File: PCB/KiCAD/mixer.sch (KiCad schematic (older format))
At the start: 12 parts

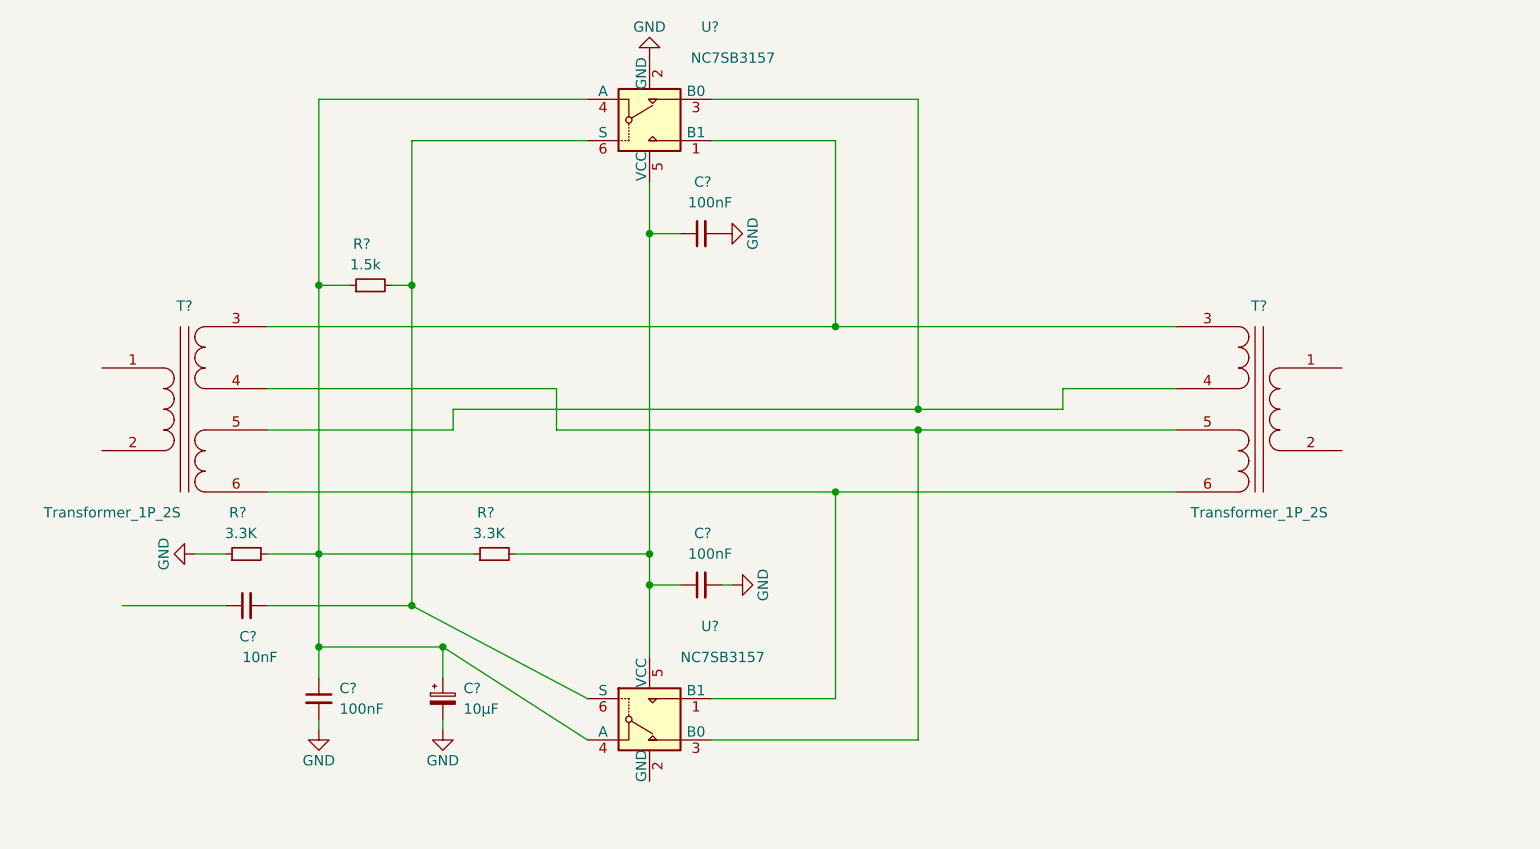
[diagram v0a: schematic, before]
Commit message: mixer schema is done, pcb progress, fix 78l06 issue
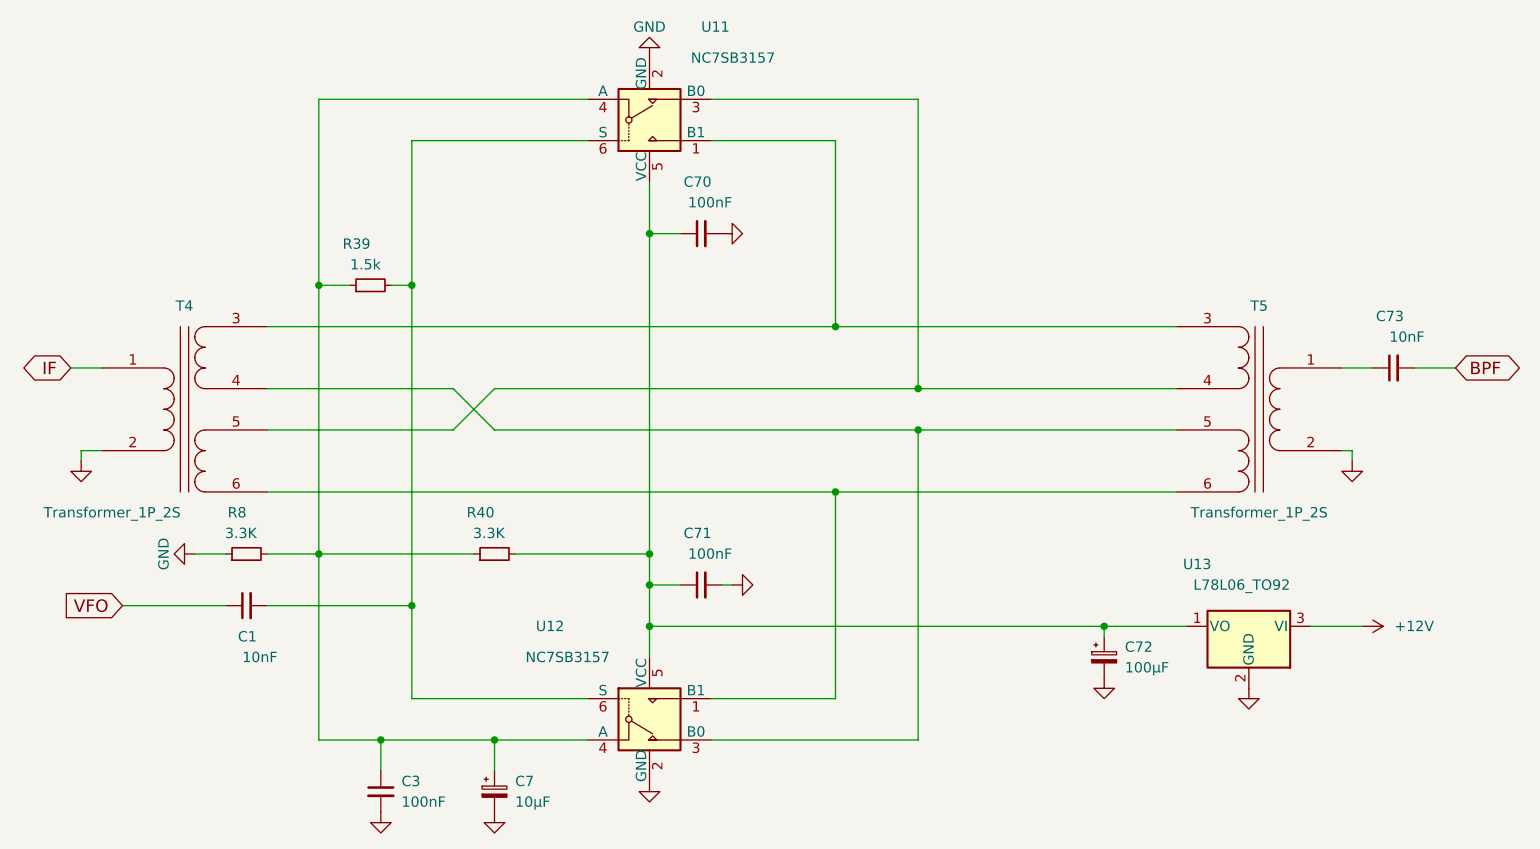
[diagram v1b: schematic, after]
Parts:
- added C72: 100µF, DragonFly:CP_Radial_D6.3mm_P2.50mm, symbol CP_Small
- added C73: 10nF, DragonFly:C_0603_HandSoldering, symbol C_Small
- added U13: L78L06_TO92, DragonFly:TO-92_Molded_Wide_Oval, symbol L78L06_TO92
- C1, C3, C70, C71: renamed from C?; footprint (none) -> DragonFly:C_0603_HandSoldering
- C7: renamed from C?; footprint (none) -> DragonFly:CP_Radial_D4.0mm_P2.00mm
- R39, R40, R8: renamed from R?; footprint (none) -> DragonFly:R_1206_0603
- T4, T5: renamed from T?; footprint (none) -> DragonFly:HF12
- U11, U12: renamed from U?; footprint (none) -> DragonFly:SOT-23-6
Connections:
- net GND: now also T4.2 (AB), T5.2 (AB), U12.2 (GND), C72.2, U13.2 (GND)
- net IF: now reaches T4.1 (AA)
- net at T5.1 (AA): now also C73.1
- net at C70.1, C71.1, R40.2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: now also C72.1, U13.1 (VO)
- net VFO: now reaches C1.1
- new net +12V: U13.3 (VI)
- new net BPF: C73.2
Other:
- moved on the sheet: C3, C7

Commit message: PCB v1.0
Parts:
- C3, C70, C71: footprint DragonFly:C_0603_HandSoldering -> DragonFly:C_1206_0603
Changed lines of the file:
@@
 Connection ~ 4850 3400
 $Comp
-L GND #PWR125
+L GND #PWR128
 U 1 1 612C19B8
 P 2650 3400
-F 0 "#PWR125" H 2650 3150 50  0001 C CNN
+F 0 "#PWR128" H 2650 3150 50  0001 C CNN
 F 1 "GND" H 2650 3250 50  0000 C CNN
 F 2 "" H 2650 3400 50  0001 C CNN
@@
 F 0 "C71" V 5350 3500 50  0000 L CNN
 F 1 "100nF" V 5250 3400 50  0000 L CNN
-F 2 "DragonFly:C_0603_HandSoldering" H 5100 3550 50  0001 C CNN
+F 2 "DragonFly:C_1206_0603" H 5100 3550 50  0001 C CNN
 F 3 "" H 5100 3550 50  0001 C CNN
 	1    5100 3550
@@
 $EndComp
 $Comp
-L GND #PWR131
+L GND #PWR134
 U 1 1 612C2F5C
 P 5250 3550
-F 0 "#PWR131" H 5250 3300 50  0001 C CNN
+F 0 "#PWR134" H 5250 3300 50  0001 C CNN
 F 1 "GND" H 5250 3400 50  0001 C CNN
 F 2 "" H 5250 3550 50  0001 C CNN
@@
 F 0 "C70" V 5350 1800 50  0000 L CNN
 F 1 "100nF" V 5250 1700 50  0000 L CNN
-F 2 "DragonFly:C_0603_HandSoldering" H 5100 1850 50  0001 C CNN
+F 2 "DragonFly:C_1206_0603" H 5100 1850 50  0001 C CNN
 F 3 "" H 5100 1850 50  0001 C CNN
 	1    5100 1850
@@
 	5150 1400 5750 1400
 $Comp
-L GND #PWR130
+L GND #PWR133
 U 1 1 612C37A6
 P 5200 1850
-F 0 "#PWR130" H 5200 1600 50  0001 C CNN
+F 0 "#PWR133" H 5200 1600 50  0001 C CNN
 F 1 "GND" H 5200 1700 50  0001 C CNN
 F 2 "" H 5200 1850 50  0001 C CNN
@@
 	3700 1400 4550 1400
 $Comp
-L GND #PWR128
+L GND #PWR131
 U 1 1 612C38C3
 P 4850 1000
-F 0 "#PWR128" H 4850 750 50  0001 C CNN
+F 0 "#PWR131" H 4850 750 50  0001 C CNN
 F 1 "GND" H 4850 850 50  0000 C CNN
 F 2 "" H 4850 1000 50  0001 C CNN
@@
 	2050 2500 2200 2500
 $Comp
-L GND #PWR124
+L GND #PWR127
 U 1 1 612C7046
 P 2100 2950
-F 0 "#PWR124" H 2100 2700 50  0001 C CNN
+F 0 "#PWR127" H 2100 2700 50  0001 C CNN
 F 1 "GND" H 2100 2800 50  0001 C CNN
 F 2 "" H 2100 2950 50  0001 C CNN
@@
 	2100 2900 2200 2900
 $Comp
-L GND #PWR134
+L GND #PWR137
 U 1 1 612C70EC
 P 8250 2950
-F 0 "#PWR134" H 8250 2700 50  0001 C CNN
+F 0 "#PWR137" H 8250 2700 50  0001 C CNN
 F 1 "GND" H 8250 2800 50  0001 C CNN
 F 2 "" H 8250 2950 50  0001 C CNN
@@
 	8250 2900 8200 2900
 $Comp
-L GND #PWR129
+L GND #PWR132
 U 1 1 612C7167
 P 4850 4500
-F 0 "#PWR129" H 4850 4250 50  0001 C CNN
+F 0 "#PWR132" H 4850 4250 50  0001 C CNN
 F 1 "GND" H 4850 4350 50  0001 C CNN
 F 2 "" H 4850 4500 50  0001 C CNN
@@
 F 0 "C3" H 3650 4600 50  0000 L CNN
 F 1 "100nF" H 3650 4500 50  0000 L CNN
-F 2 "DragonFly:C_0603_HandSoldering" H 3550 4550 50  0001 C CNN
+F 2 "DragonFly:C_1206_0603" H 3550 4550 50  0001 C CNN
 F 3 "" H 3550 4550 50  0001 C CNN
 	1    3550 4550
@@
 Connection ~ 3550 4300
 $Comp
-L GND #PWR127
+L GND #PWR130
 U 1 1 612C7874
 P 4100 4650
-F 0 "#PWR127" H 4100 4400 50  0001 C CNN
+F 0 "#PWR130" H 4100 4400 50  0001 C CNN
 F 1 "GND" H 4100 4500 50  0001 C CNN
 F 2 "" H 4100 4650 50  0001 C CNN
@@
 $EndComp
 $Comp
-L GND #PWR126
+L GND #PWR129
 U 1 1 612C78A6
 P 3550 4650
-F 0 "#PWR126" H 3550 4400 50  0001 C CNN
+F 0 "#PWR129" H 3550 4400 50  0001 C CNN
 F 1 "GND" H 3550 4500 50  0001 C CNN
 F 2 "" H 3550 4650 50  0001 C CNN
@@
 Connection ~ 4850 3750
 $Comp
-L GND #PWR133
+L GND #PWR136
 U 1 1 612C940C
 P 7750 4050
-F 0 "#PWR133" H 7750 3800 50  0001 C CNN
+F 0 "#PWR136" H 7750 3800 50  0001 C CNN
 F 1 "GND" H 7750 3900 50  0001 C CNN
 F 2 "" H 7750 4050 50  0001 C CNN
@@
 $EndComp
 $Comp
-L GND #PWR132
+L GND #PWR135
 U 1 1 612C9675
 P 7050 4000
-F 0 "#PWR132" H 7050 3750 50  0001 C CNN
+F 0 "#PWR135" H 7050 3750 50  0001 C CNN
 F 1 "GND" H 7050 3850 50  0001 C CNN
 F 2 "" H 7050 4000 50  0001 C CNN
@@
 	8050 3750 8300 3750
 $Comp
-L +12V #PWR135
+L +12V #PWR138
 U 1 1 612C97BE
 P 8300 3750
-F 0 "#PWR135" H 8300 3600 50  0001 C CNN
+F 0 "#PWR138" H 8300 3600 50  0001 C CNN
 F 1 "+12V" V 8300 4000 50  0000 C CNN
 F 2 "" H 8300 3750 50  0001 C CNN

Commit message: PCB production
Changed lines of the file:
@@
 P 2600 2700
 F 0 "T4" H 2600 3200 50  0000 C CNN
-F 1 "Transformer_1P_2S" H 2250 2200 50  0000 C CNN
+F 1 "Transformer_1P_2S" H 2250 2200 50  0001 C CNN
 F 2 "DragonFly:HF12" H 2600 2700 50  0001 C CNN
 F 3 "" H 2600 2700 50  0001 C CNN
@@
 P 7800 2700
 F 0 "T5" H 7800 3200 50  0000 C CNN
-F 1 "Transformer_1P_2S" H 7800 2200 50  0000 C CNN
+F 1 "Transformer_1P_2S" H 7800 2200 50  0001 C CNN
 F 2 "DragonFly:HF12" H 7800 2700 50  0001 C CNN
 F 3 "" H 7800 2700 50  0001 C CNN
@@
 Connection ~ 4850 3400
 $Comp
-L GND #PWR128
+L GND #PWR0127
 U 1 1 612C19B8
 P 2650 3400
-F 0 "#PWR128" H 2650 3150 50  0001 C CNN
+F 0 "#PWR0127" H 2650 3150 50  0001 C CNN
 F 1 "GND" H 2650 3250 50  0000 C CNN
 F 2 "" H 2650 3400 50  0001 C CNN
@@
 $EndComp
 $Comp
-L GND #PWR134
+L GND #PWR0128
 U 1 1 612C2F5C
 P 5250 3550
-F 0 "#PWR134" H 5250 3300 50  0001 C CNN
+F 0 "#PWR0128" H 5250 3300 50  0001 C CNN
 F 1 "GND" H 5250 3400 50  0001 C CNN
 F 2 "" H 5250 3550 50  0001 C CNN
@@
 	5150 1400 5750 1400
 $Comp
-L GND #PWR133
+L GND #PWR0129
 U 1 1 612C37A6
 P 5200 1850
-F 0 "#PWR133" H 5200 1600 50  0001 C CNN
+F 0 "#PWR0129" H 5200 1600 50  0001 C CNN
 F 1 "GND" H 5200 1700 50  0001 C CNN
 F 2 "" H 5200 1850 50  0001 C CNN
@@
 	3700 1400 4550 1400
 $Comp
-L GND #PWR131
+L GND #PWR0130
 U 1 1 612C38C3
 P 4850 1000
-F 0 "#PWR131" H 4850 750 50  0001 C CNN
+F 0 "#PWR0130" H 4850 750 50  0001 C CNN
 F 1 "GND" H 4850 850 50  0000 C CNN
 F 2 "" H 4850 1000 50  0001 C CNN
@@
 	2050 2500 2200 2500
 $Comp
-L GND #PWR127
+L GND #PWR0131
 U 1 1 612C7046
 P 2100 2950
-F 0 "#PWR127" H 2100 2700 50  0001 C CNN
+F 0 "#PWR0131" H 2100 2700 50  0001 C CNN
 F 1 "GND" H 2100 2800 50  0001 C CNN
 F 2 "" H 2100 2950 50  0001 C CNN
@@
 	2100 2900 2200 2900
 $Comp
-L GND #PWR137
+L GND #PWR0132
 U 1 1 612C70EC
 P 8250 2950
-F 0 "#PWR137" H 8250 2700 50  0001 C CNN
+F 0 "#PWR0132" H 8250 2700 50  0001 C CNN
 F 1 "GND" H 8250 2800 50  0001 C CNN
 F 2 "" H 8250 2950 50  0001 C CNN
@@
 	8250 2900 8200 2900
 $Comp
-L GND #PWR132
+L GND #PWR0133
 U 1 1 612C7167
 P 4850 4500
-F 0 "#PWR132" H 4850 4250 50  0001 C CNN
+F 0 "#PWR0133" H 4850 4250 50  0001 C CNN
 F 1 "GND" H 4850 4350 50  0001 C CNN
 F 2 "" H 4850 4500 50  0001 C CNN
@@
 Connection ~ 3550 4300
 $Comp
-L GND #PWR130
+L GND #PWR0134
 U 1 1 612C7874
 P 4100 4650
-F 0 "#PWR130" H 4100 4400 50  0001 C CNN
+F 0 "#PWR0134" H 4100 4400 50  0001 C CNN
 F 1 "GND" H 4100 4500 50  0001 C CNN
 F 2 "" H 4100 4650 50  0001 C CNN
@@
 $EndComp
 $Comp
-L GND #PWR129
+L GND #PWR0135
 U 1 1 612C78A6
 P 3550 4650
-F 0 "#PWR129" H 3550 4400 50  0001 C CNN
+F 0 "#PWR0135" H 3550 4400 50  0001 C CNN
 F 1 "GND" H 3550 4500 50  0001 C CNN
 F 2 "" H 3550 4650 50  0001 C CNN
@@
 Connection ~ 4850 3750
 $Comp
-L GND #PWR136
+L GND #PWR0136
 U 1 1 612C940C
 P 7750 4050
-F 0 "#PWR136" H 7750 3800 50  0001 C CNN
+F 0 "#PWR0136" H 7750 3800 50  0001 C CNN
 F 1 "GND" H 7750 3900 50  0001 C CNN
 F 2 "" H 7750 4050 50  0001 C CNN
@@
 $EndComp
 $Comp
-L GND #PWR135
+L GND #PWR0137
 U 1 1 612C9675
 P 7050 4000
-F 0 "#PWR135" H 7050 3750 50  0001 C CNN
+F 0 "#PWR0137" H 7050 3750 50  0001 C CNN
 F 1 "GND" H 7050 3850 50  0001 C CNN
 F 2 "" H 7050 4000 50  0001 C CNN
@@
 	8050 3750 8300 3750
 $Comp
-L +12V #PWR138
+L +12V #PWR0138
 U 1 1 612C97BE
 P 8300 3750
-F 0 "#PWR138" H 8300 3600 50  0001 C CNN
+F 0 "#PWR0138" H 8300 3600 50  0001 C CNN
 F 1 "+12V" V 8300 4000 50  0000 C CNN
 F 2 "" H 8300 3750 50  0001 C CNN
